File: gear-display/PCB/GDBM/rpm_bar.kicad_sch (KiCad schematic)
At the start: 29 parts

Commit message: updates
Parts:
- removed R? (x13): R_0805_1200_5%, KD_Resistor:R_0805_2012Metric, symbol KD_Resistor:R_0805_1200_5%
- added R? (x7): R_1206_383_1%, KD_Resistor:RESC3216X70N, symbol KD_Resistor:R_1206_383_1%
- added R? (x3): R_1206_191_1%, KD_Resistor:RESC3216X70N, symbol KD_Resistor:R_1206_191_1%
- added R? (x3): R_1206_110_1%, KD_Resistor:RESC3216X70N, symbol KD_Resistor:R_1206_110_1%
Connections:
- net at D?.2 (A): now also R?.2 (x13)
- net at Q?.4 (S): now also R?.1, R?.1, R?.1, R?.1, R?.1, R?.1, R?.1, R?.1, R?.1, R?.1, R?.1, R?.1, R?.1
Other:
- note added: "Green: Vf: 3.3 V (Max 4.1 V) Intensity: 178 mcd (min 70 mcd) @ 20 mA -> 380 Ohm"
- note added: "Red: Vf: 1.95 V (Max 2.5 V) Intensity: 29 mcd (min 12 mcd) @ 20 mA -> 110 Ohm"
- note added: "Yellow: Vf: 2 V (Max 2.5 V) Intensity: 49 mcd (min 20 mcd) @ 20 mA -> 190 Ohm"

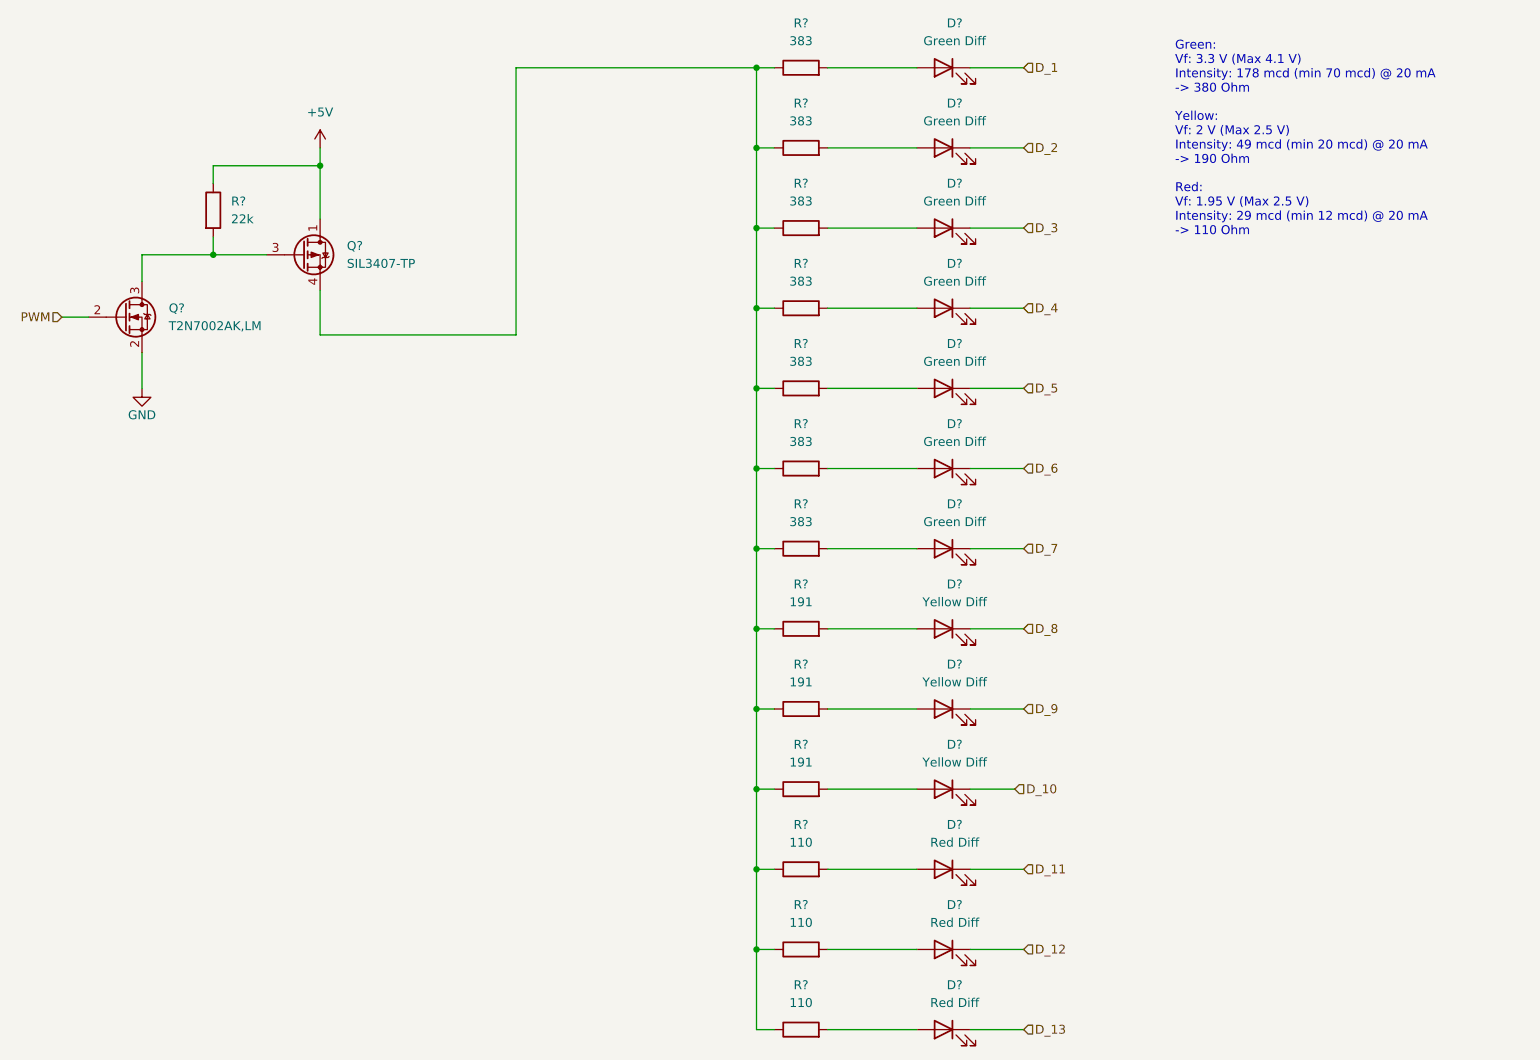
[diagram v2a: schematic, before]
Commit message: changed to match simhub conf
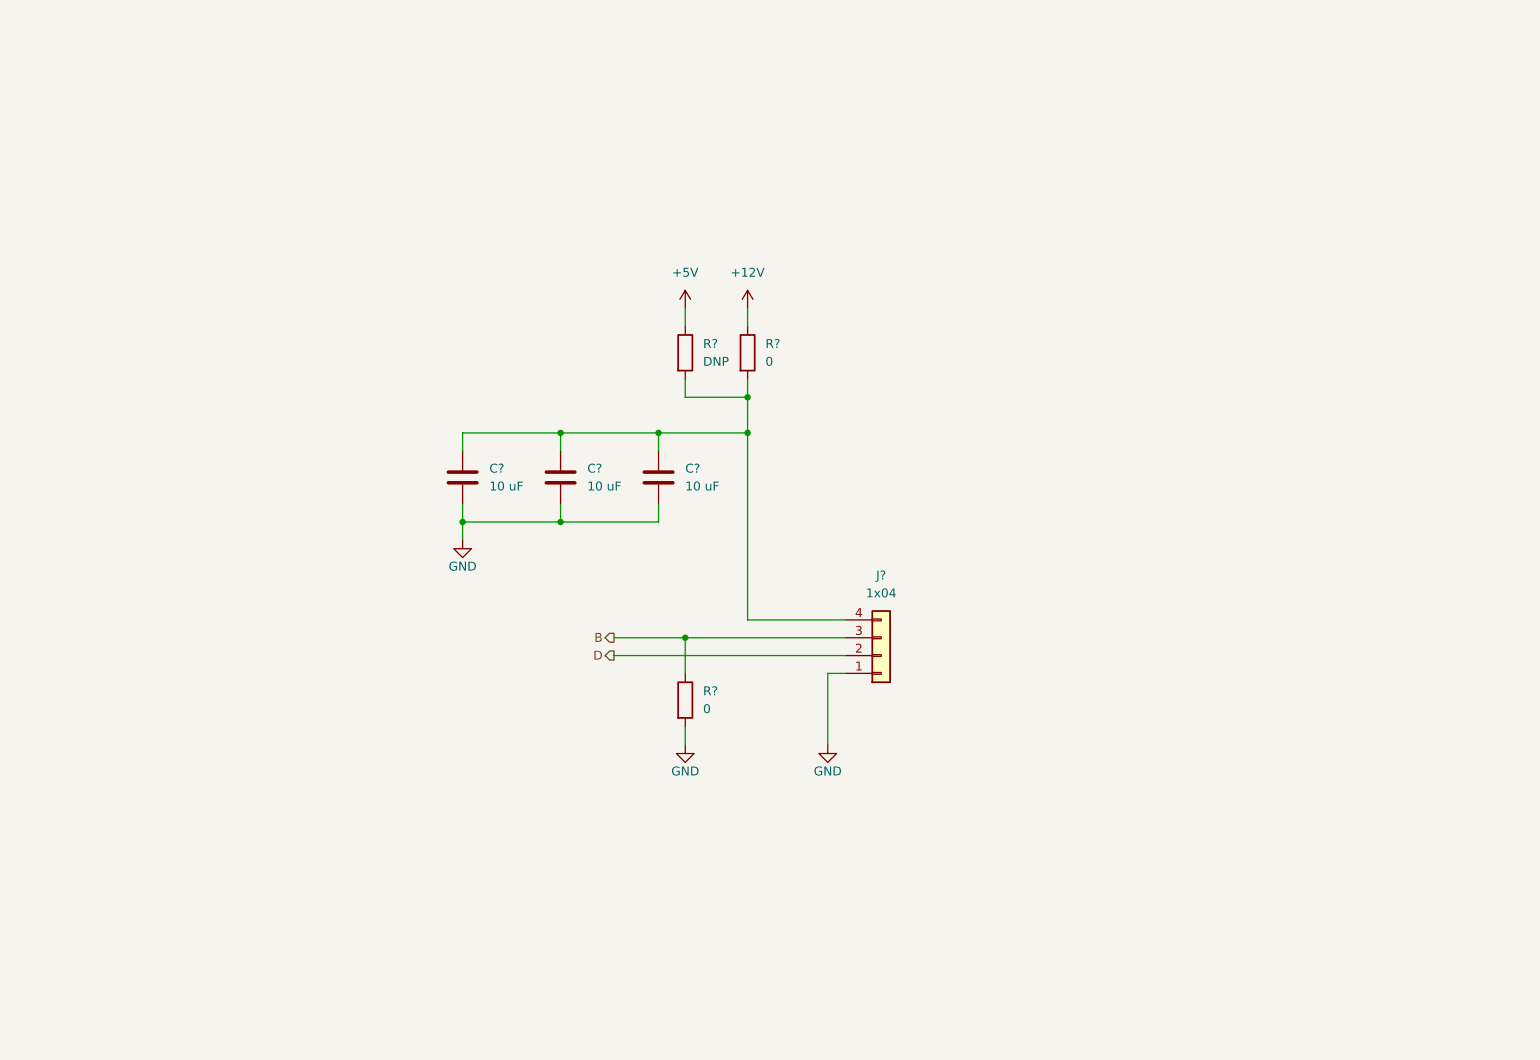
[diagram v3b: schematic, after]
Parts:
- removed D? (x7): TH_Rectangular_5mm_Green_525nm_Diff_XSDG23MB, KD_Diode:LED_RECT_5.0mm_SunLED_XSDG23MB, symbol KD_Led:TH_Rectangular_5mm_Green_525nm_Diff_XSDG23MB
- removed D? (x3): TH_Rectangular_5mm_Yellow_590nm_Diff_XSMYK23MB, KD_Diode:LED_RECT_5.0mm_SunLED_XSDG23MB, symbol KD_Led:TH_Rectangular_5mm_Yellow_590nm_Diff_XSMYK23MB
- removed D? (x3): TH_Rectangular_5mm_Red_630nm_Diff_XSMDK23MB, KD_Diode:LED_RECT_5.0mm_SunLED_XSDG23MB, symbol KD_Led:TH_Rectangular_5mm_Red_630nm_Diff_XSMDK23MB
- removed Q?: NMOS_60V_200mA_T2N7002AK_LM, KD_Package_TO_SOT_SMD:SOT95P230X100-3N, symbol KD_Transistor_FET:NMOS_60V_200mA_T2N7002AK_LM
- removed Q?: PMOS_30V_4A1_SIL3407-TP, KD_Package_TO_SOT_SMD:SOT95P280X120-6RN, symbol KD_Transistor_FET:PMOS_30V_4A1_SIL3407-TP
- removed R? (x7): R_1206_383_1%, KD_Resistor:RESC3216X70N, symbol KD_Resistor:R_1206_383_1%
- removed R? (x3): R_1206_191_1%, KD_Resistor:RESC3216X70N, symbol KD_Resistor:R_1206_191_1%
- removed R? (x3): R_1206_110_1%, KD_Resistor:RESC3216X70N, symbol KD_Resistor:R_1206_110_1%
- removed R?: R_0603_22k_1%, KD_Resistor:R_0603_1608Metric, symbol KD_Resistor:R_0603_22k_1%
- added C? (x3): C_1206_10u_50V, KD_Capacitor:C_1206_3216Metric, symbol KD_Capacitor:C_1206_10u_50V
- added J?: Con_Screw_1x04_691313510004, KD_Connector_Screw:CON_508_1X04_691313510004_Mated, symbol KD_Connector_Screw:Con_Screw_1x04_691313510004
- added R? (x2): R_0805_0_automotive, KD_Resistor:R_0805_2012Metric, symbol KD_Resistor:R_0805_0_automotive
- added R?: R_0805_DNP, KD_Resistor:RESC2012X60N_DNP, symbol KD_Resistor:R_0805_DNP
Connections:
- net +5V: now also R?.1
- net GND: now also C?.2, C?.2, C?.2, J?.1 (Pin_1), R?.2
- new net: C?.1, C?.1, C?.1, J?.4 (Pin_4), R?.2, R?.2
- new net +12V: R?.1
- new net B: J?.3 (Pin_3), R?.1
- new net D: J?.2 (Pin_2)
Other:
- note removed: "Green: Vf: 3.3 V (Max 4.1 V) Intensity: 178 mcd (min 70 mcd) @ 20 mA -> 380 Ohm"
- note removed: "Red: Vf: 1.95 V (Max 2.5 V) Intensity: 29 mcd (min 12 mcd) @ 20 mA -> 110 Ohm"
- note removed: "Yellow: Vf: 2 V (Max 2.5 V) Intensity: 49 mcd (min 20 mcd) @ 20 mA -> 190 Ohm"

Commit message: rikki
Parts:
- R21, R22: renamed from R?; footprint KD_Resistor:R_0805_2012Metric -> KD_Resistor:RESC2012X60N
- gave numbers to parts that had none: 5
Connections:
- net B renamed LED_STRIP_B
- net D renamed LED_STRIP_D
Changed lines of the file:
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@@
   (title_block
     (title "Gear Display Board")
-    (date "2022-08-07")
+    (date "2022-08-13")
     (rev "1.0")
     (company "Kallio Designs Oy")
     (comment 1 "Teemu Latonen")
-    (comment 2 "ASSEMBLY_PN")
-    (comment 3 "PCB_PN")
+    (comment 2 "000064")
+    (comment 3 "000065")
   )
   (junction (at 143.51 106.68) (diameter 0) (color 0 0 0 0)
@@
     (stroke (width 0) (type default) (color 0 0 0 0))
   )
-  (hierarchical_label "B" (shape output) (at 133.35 106.68 180)
+  (hierarchical_label "LED_STRIP_B" (shape output) (at 133.35 106.68 180)
     (effects (font (size 1.27 1.27)) (justify right))
   )
-  (hierarchical_label "D" (shape output) (at 133.35 109.22 180)
+  (hierarchical_label "LED_STRIP_D" (shape output) (at 133.35 109.22 180)
     (effects (font (size 1.27 1.27)) (justify right))
   )
   (symbol (lib_id "KD_Resistor:R_0805_0_automotive") (at 152.4 66.04 0) (unit 1)
     (in_bom yes) (on_board yes) (fields_autoplaced)
-    (property "Reference" "R?" (id 0) (at 154.94 64.7699 0)
+    (property "Reference" "R22" (id 0) (at 154.94 64.7699 0)
       (effects (font (size 1.27 1.27)) (justify left))
     )
@@
       (effects (font (size 1.27 1.27)) (justify left) hide)
     )
-    (property "Footprint" "KD_Resistor:R_0805_2012Metric" (id 2) (at 139.7 52.07 0)
+    (property "Footprint" "KD_Resistor:RESC2012X60N" (id 2) (at 139.7 52.07 0)
       (effects (font (size 1.27 1.27)) (justify left) hide)
     )
@@
   (symbol (lib_id "KD_Capacitor:C_1206_10u_50V") (at 111.76 83.82 0) (unit 1)
     (in_bom yes) (on_board yes) (fields_autoplaced)
-    (property "Reference" "C?" (id 0) (at 115.57 82.5499 0)
+    (property "Reference" "C16" (id 0) (at 115.57 82.5499 0)
       (effects (font (size 1.27 1.27)) (justify left))
     )
@@
   (symbol (lib_id "power:+5V") (at 143.51 59.69 0) (unit 1)
     (in_bom yes) (on_board yes) (fields_autoplaced)
-    (property "Reference" "#PWR?" (id 0) (at 143.51 63.5 0)
+    (property "Reference" "#PWR0125" (id 0) (at 143.51 63.5 0)
       (effects (font (size 1.27 1.27)) hide)
     )
@@
   (symbol (lib_id "KD_Capacitor:C_1206_10u_50V") (at 139.7 83.82 0) (unit 1)
     (in_bom yes) (on_board yes) (fields_autoplaced)
-    (property "Reference" "C?" (id 0) (at 143.51 82.5499 0)
+    (property "Reference" "C18" (id 0) (at 143.51 82.5499 0)
       (effects (font (size 1.27 1.27)) (justify left))
     )
@@
   (symbol (lib_id "KD_Resistor:R_0805_0_automotive") (at 143.51 115.57 0) (unit 1)
     (in_bom yes) (on_board yes) (fields_autoplaced)
-    (property "Reference" "R?" (id 0) (at 146.05 114.2999 0)
+    (property "Reference" "R21" (id 0) (at 146.05 114.2999 0)
       (effects (font (size 1.27 1.27)) (justify left))
     )
@@
       (effects (font (size 1.27 1.27)) (justify left) hide)
     )
-    (property "Footprint" "KD_Resistor:R_0805_2012Metric" (id 2) (at 130.81 101.6 0)
+    (property "Footprint" "KD_Resistor:RESC2012X60N" (id 2) (at 130.81 101.6 0)
       (effects (font (size 1.27 1.27)) (justify left) hide)
     )
@@
   (symbol (lib_id "power:GND") (at 163.83 121.92 0) (unit 1)
     (in_bom yes) (on_board yes)
-    (property "Reference" "#PWR?" (id 0) (at 163.83 128.27 0)
+    (property "Reference" "#PWR0122" (id 0) (at 163.83 128.27 0)
       (effects (font (size 1.27 1.27)) hide)
     )
@@
   (symbol (lib_id "power:GND") (at 143.51 121.92 0) (unit 1)
     (in_bom yes) (on_board yes)
-    (property "Reference" "#PWR?" (id 0) (at 143.51 128.27 0)
+    (property "Reference" "#PWR0123" (id 0) (at 143.51 128.27 0)
       (effects (font (size 1.27 1.27)) hide)
     )
@@
   (symbol (lib_id "KD_Connector_Screw:Con_Screw_1x04_691313510004") (at 166.37 111.76 0) (mirror x) (unit 1)
     (in_bom yes) (on_board yes) (fields_autoplaced)
-    (property "Reference" "J?" (id 0) (at 171.45 97.79 0))
+    (property "Reference" "J4" (id 0) (at 171.45 97.79 0))
     (property "Value" "Con_Screw_1x04_691313510004" (id 1) (at 153.67 143.51 0)
       (effects (font (size 1.27 1.27)) (justify left) hide)
@@
   (symbol (lib_id "power:+12V") (at 152.4 59.69 0) (unit 1)
     (in_bom yes) (on_board yes) (fields_autoplaced)
-    (property "Reference" "#PWR?" (id 0) (at 152.4 63.5 0)
+    (property "Reference" "#PWR0126" (id 0) (at 152.4 63.5 0)
       (effects (font (size 1.27 1.27)) hide)
     )
@@
   (symbol (lib_id "KD_Resistor:R_0805_DNP") (at 143.51 66.04 0) (unit 1)
     (in_bom yes) (on_board yes) (fields_autoplaced)
-    (property "Reference" "R?" (id 0) (at 146.05 64.7699 0)
+    (property "Reference" "R20" (id 0) (at 146.05 64.7699 0)
       (effects (font (size 1.27 1.27)) (justify left))
     )
@@
   (symbol (lib_id "power:GND") (at 111.76 92.71 0) (unit 1)
     (in_bom yes) (on_board yes)
-    (property "Reference" "#PWR?" (id 0) (at 111.76 99.06 0)
+    (property "Reference" "#PWR0124" (id 0) (at 111.76 99.06 0)
       (effects (font (size 1.27 1.27)) hide)
     )
@@
   (symbol (lib_id "KD_Capacitor:C_1206_10u_50V") (at 125.73 83.82 0) (unit 1)
     (in_bom yes) (on_board yes) (fields_autoplaced)
-    (property "Reference" "C?" (id 0) (at 129.54 82.5499 0)
-      (effects (font (size 1.27 1.27)) (justify left))
-    )
+    (property "Reference" "C17" (id 0) (at 129.54 82.5499 0)
+      (effects (font (size 1.27 1.27)) (justify left))
+    )
